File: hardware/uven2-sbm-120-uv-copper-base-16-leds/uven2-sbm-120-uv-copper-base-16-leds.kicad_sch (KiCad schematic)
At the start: 60 parts, among them J1 LED0+, J10 LED4-, J11 LED5+, J12 LED5-, J13 LED6+, J14 LED6-, J15 LED7+, J16 LED7-, J17 LED8+, J18 LED8-, J19 LED9+, J2 LED0-, J20 LED9-, J21 LED10+, J22 LED10-, J23 LED11+, J24 LED11-, J25 LED12+, J26 LED12-, J27 LED13+, J28 LED13-, J29 LED14+, J3 LED1+, J30 LED14-, J31 LED15+, J32 LED15-, J4 LED1-, J5 LED2+, J6 LED2-, J7 LED3+, J8 LED3-, J9 LED4+, U1 SBM-120-UV, U10 SBM-120-UV, U11 SBM-120-UV, U12 SBM-120-UV, U13 SBM-120-UV, U14 SBM-120-UV, U15 SBM-120-UV, U16 SBM-120-UV, U2 SBM-120-UV, U3 SBM-120-UV, U4 SBM-120-UV, U5 SBM-120-UV, U6 SBM-120-UV, U7 SBM-120-UV, U8 SBM-120-UV, U9 SBM-120-UV

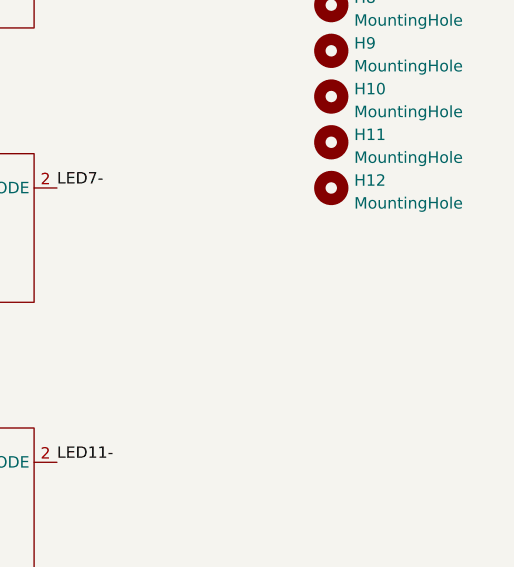
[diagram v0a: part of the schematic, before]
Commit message: more mounting holes
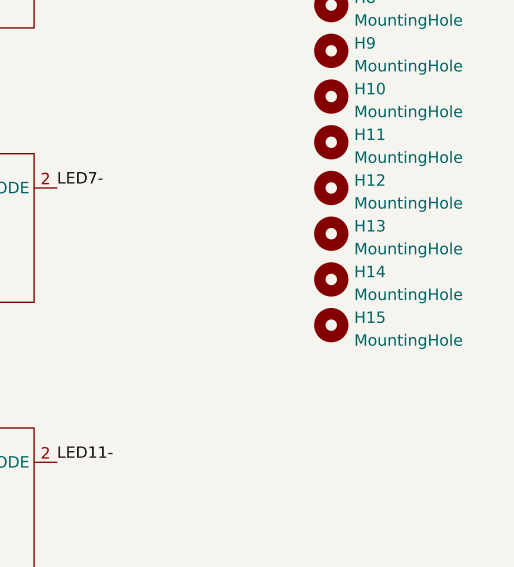
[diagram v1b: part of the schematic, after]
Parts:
- added H13, H14, H15: MountingHole, MountingHole:MountingHole_3.2mm_M3, symbol Mechanical:MountingHole
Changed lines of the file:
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@@
     (effects (font (size 1.27 1.27)) (justify left bottom))
+  )
+  (symbol (lib_id "Mechanical:MountingHole") (at 259.08 91.44 0) (unit 1)
+    (in_bom yes) (on_board yes) (fields_autoplaced)
+    (property "Reference" "H15" (id 0) (at 261.62 90.6053 0)
+      (effects (font (size 1.27 1.27)) (justify left))
+    )
+    (property "Value" "MountingHole" (id 1) (at 261.62 93.1422 0)
+      (effects (font (size 1.27 1.27)) (justify left))
+    )
+    (property "Footprint" "MountingHole:MountingHole_3.2mm_M3" (id 2) (at 259.08 91.44 0)
+      (effects (font (size 1.27 1.27)) hide)
+    )
+    (property "Datasheet" "~" (id 3) (at 259.08 91.44 0)
+      (effects (font (size 1.27 1.27)) hide)
+    )
   )
   (symbol (lib_id "custom:SBM-120-UV") (at 215.9 50.8 0) (unit 1)
@@
     (pin "1")
   )
+  (symbol (lib_id "Mechanical:MountingHole") (at 259.08 86.36 0) (unit 1)
+    (in_bom yes) (on_board yes) (fields_autoplaced)
+    (property "Reference" "H14" (id 0) (at 261.62 85.5253 0)
+      (effects (font (size 1.27 1.27)) (justify left))
+    )
+    (property "Value" "MountingHole" (id 1) (at 261.62 88.0622 0)
+      (effects (font (size 1.27 1.27)) (justify left))
+    )
+    (property "Footprint" "MountingHole:MountingHole_3.2mm_M3" (id 2) (at 259.08 86.36 0)
+      (effects (font (size 1.27 1.27)) hide)
+    )
+    (property "Datasheet" "~" (id 3) (at 259.08 86.36 0)
+      (effects (font (size 1.27 1.27)) hide)
+    )
+  )
   (symbol (lib_id "Connector:Conn_01x01_Female") (at 53.34 68.58 180) (unit 1)
     (in_bom yes) (on_board yes) (fields_autoplaced)
@@
     (pin "1")
   )
+  (symbol (lib_id "Mechanical:MountingHole") (at 259.08 81.28 0) (unit 1)
+    (in_bom yes) (on_board yes) (fields_autoplaced)
+    (property "Reference" "H13" (id 0) (at 261.62 80.4453 0)
+      (effects (font (size 1.27 1.27)) (justify left))
+    )
+    (property "Value" "MountingHole" (id 1) (at 261.62 82.9822 0)
+      (effects (font (size 1.27 1.27)) (justify left))
+    )
+    (property "Footprint" "MountingHole:MountingHole_3.2mm_M3" (id 2) (at 259.08 81.28 0)
+      (effects (font (size 1.27 1.27)) hide)
+    )
+    (property "Datasheet" "~" (id 3) (at 259.08 81.28 0)
+      (effects (font (size 1.27 1.27)) hide)
+    )
+  )
   (symbol (lib_id "Connector:Conn_01x01_Female") (at 53.34 43.18 180) (unit 1)
     (in_bom yes) (on_board yes) (fields_autoplaced)
@@
       (reference "H12") (unit 1) (value "MountingHole") (footprint "MountingHole:MountingHole_3.2mm_M3")
     )
+    (path "/480cf691-721f-4899-bd8b-114328ed6cb5"
+      (reference "H13") (unit 1) (value "MountingHole") (footprint "MountingHole:MountingHole_3.2mm_M3")
+    )
+    (path "/1b30173e-3e23-4824-b9c7-bba22dbc95f5"
+      (reference "H14") (unit 1) (value "MountingHole") (footprint "MountingHole:MountingHole_3.2mm_M3")
+    )
+    (path "/0d2686f8-8d34-493a-8a4f-3bd8bf6ef14b"
+      (reference "H15") (unit 1) (value "MountingHole") (footprint "MountingHole:MountingHole_3.2mm_M3")
+    )
     (path "/babefa49-307d-4cb6-8ca1-f2ed9a23079d"

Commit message: with thermistors
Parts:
- added H? (x5): MountingHole, MountingHole:MountingHole_3.2mm_M3, symbol Mechanical:MountingHole
- added J34: TEMP_LED0, TestPoint:TestPoint_Pad_2.0x2.0mm, symbol Connector:Conn_01x01_Female
- added J35: TEMP_LED1, TestPoint:TestPoint_Pad_2.0x2.0mm, symbol Connector:Conn_01x01_Female
- added J36: TEMP_LED2, TestPoint:TestPoint_Pad_2.0x2.0mm, symbol Connector:Conn_01x01_Female
- added J37: TEMP_LED3, TestPoint:TestPoint_Pad_2.0x2.0mm, symbol Connector:Conn_01x01_Female
- added J38: TEMP_LED4, TestPoint:TestPoint_Pad_2.0x2.0mm, symbol Connector:Conn_01x01_Female
- added J39: TEMP_LED5, TestPoint:TestPoint_Pad_2.0x2.0mm, symbol Connector:Conn_01x01_Female
- added J40: TEMP_LED6, TestPoint:TestPoint_Pad_2.0x2.0mm, symbol Connector:Conn_01x01_Female
- added J41: TEMP_LED7, TestPoint:TestPoint_Pad_2.0x2.0mm, symbol Connector:Conn_01x01_Female
- added J42: TEMP_LED8, TestPoint:TestPoint_Pad_2.0x2.0mm, symbol Connector:Conn_01x01_Female
- added J43: TEMP_LED9, TestPoint:TestPoint_Pad_2.0x2.0mm, symbol Connector:Conn_01x01_Female
- added J44: TEMP_LED10, TestPoint:TestPoint_Pad_2.0x2.0mm, symbol Connector:Conn_01x01_Female
- added J45: TEMP_LED11, TestPoint:TestPoint_Pad_2.0x2.0mm, symbol Connector:Conn_01x01_Female
- added J46: TEMP_LED12, TestPoint:TestPoint_Pad_2.0x2.0mm, symbol Connector:Conn_01x01_Female
- added J47: TEMP_LED13, TestPoint:TestPoint_Pad_2.0x2.0mm, symbol Connector:Conn_01x01_Female
- added J48: TEMP_LED14, TestPoint:TestPoint_Pad_2.0x2.0mm, symbol Connector:Conn_01x01_Female
- added J49: TEMP_LED15, TestPoint:TestPoint_Pad_2.0x2.0mm, symbol Connector:Conn_01x01_Female
- added J50, J51, J52, J53, J54, J55, J56, J57, J58, J59, J60, J61, J62, J63, J64, J65: GND, TestPoint:TestPoint_Pad_2.0x2.0mm, symbol Connector:Conn_01x01_Female
- added TH1, TH10, TH11, TH12, TH13, TH14, TH15, TH16, TH2, TH3, TH4, TH5, TH6, TH7, TH8, TH9: NTC, Resistor_SMD:R_0805_2012Metric_Pad1.20x1.40mm_HandSolder, symbol Device:Thermistor_NTC
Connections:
- new net: J39.1 (Pin_1), TH6.1
- new net: J36.1 (Pin_1), TH3.1
- new net: J41.1 (Pin_1), TH8.1
- new net: J43.1 (Pin_1), TH10.1
- new net: J48.1 (Pin_1), TH15.1
- new net: J47.1 (Pin_1), TH14.1
- new net: J49.1 (Pin_1), TH16.1
- new net: J44.1 (Pin_1), TH11.1
- new net: J37.1 (Pin_1), TH4.1
- new net: J40.1 (Pin_1), TH7.1
- new net: J35.1 (Pin_1), TH2.1
- new net: J38.1 (Pin_1), TH5.1
- new net: J46.1 (Pin_1), TH13.1
- new net: J34.1 (Pin_1), TH1.1
- new net: J42.1 (Pin_1), TH9.1
- new net: J45.1 (Pin_1), TH12.1
- new net GND: J50.1 (Pin_1), J51.1 (Pin_1), J52.1 (Pin_1), J53.1 (Pin_1), J54.1 (Pin_1), J55.1 (Pin_1), J56.1 (Pin_1), J57.1 (Pin_1), J58.1 (Pin_1), J59.1 (Pin_1), J60.1 (Pin_1), J61.1 (Pin_1), J62.1 (Pin_1), J63.1 (Pin_1), J64.1 (Pin_1), J65.1 (Pin_1), TH1.2, TH10.2, TH11.2, TH12.2, TH13.2, TH14.2, TH15.2, TH16.2, TH2.2, TH3.2, TH4.2, TH5.2, TH6.2, TH7.2, TH8.2, TH9.2
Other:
- moved on the sheet: J1, J10, J11, J12, J13, J14, J15, J16, J17, J18, J19, J2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

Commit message: with thermistors
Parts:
- gave numbers to parts that had none: 5
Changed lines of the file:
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@@
   (symbol (lib_id "Mechanical:MountingHole") (at 259.08 107.315 0) (unit 1)
     (in_bom yes) (on_board yes) (fields_autoplaced)
-    (property "Reference" "H?" (id 0) (at 261.62 106.4803 0)
+    (property "Reference" "H18" (id 0) (at 261.62 106.4803 0)
       (effects (font (size 1.27 1.27)) (justify left))
     )
@@
   (symbol (lib_id "Mechanical:MountingHole") (at 259.08 97.155 0) (unit 1)
     (in_bom yes) (on_board yes) (fields_autoplaced)
-    (property "Reference" "H?" (id 0) (at 261.62 96.3203 0)
+    (property "Reference" "H16" (id 0) (at 261.62 96.3203 0)
       (effects (font (size 1.27 1.27)) (justify left))
     )
@@
   (symbol (lib_id "Mechanical:MountingHole") (at 259.08 112.395 0) (unit 1)
     (in_bom yes) (on_board yes) (fields_autoplaced)
-    (property "Reference" "H?" (id 0) (at 261.62 111.5603 0)
+    (property "Reference" "H19" (id 0) (at 261.62 111.5603 0)
       (effects (font (size 1.27 1.27)) (justify left))
     )
@@
   (symbol (lib_id "Mechanical:MountingHole") (at 259.08 117.475 0) (unit 1)
     (in_bom yes) (on_board yes) (fields_autoplaced)
-    (property "Reference" "H?" (id 0) (at 261.62 116.6403 0)
+    (property "Reference" "H20" (id 0) (at 261.62 116.6403 0)
       (effects (font (size 1.27 1.27)) (justify left))
     )
@@
   (symbol (lib_id "Mechanical:MountingHole") (at 259.08 102.235 0) (unit 1)
     (in_bom yes) (on_board yes) (fields_autoplaced)
-    (property "Reference" "H?" (id 0) (at 261.62 101.4003 0)
+    (property "Reference" "H17" (id 0) (at 261.62 101.4003 0)
       (effects (font (size 1.27 1.27)) (justify left))
     )
@@
       (reference "H15") (unit 1) (value "MountingHole") (footprint "MountingHole:MountingHole_3.2mm_M3")
     )
+    (path "/741716d0-a841-4c1f-b24a-95f2ab48fc46"
+      (reference "H16") (unit 1) (value "MountingHole") (footprint "MountingHole:MountingHole_3.2mm_M3")
+    )
+    (path "/f5f59cc5-295d-452f-b22c-723c92bfdb2b"
+      (reference "H17") (unit 1) (value "MountingHole") (footprint "MountingHole:MountingHole_3.2mm_M3")
+    )
     (path "/1be9032b-da63-43b5-b4d8-9b92c8dcb60c"
-      (reference "H?") (unit 1) (value "MountingHole") (footprint "MountingHole:MountingHole_3.2mm_M3")
-    )
-    (path "/741716d0-a841-4c1f-b24a-95f2ab48fc46"
-      (reference "H?") (unit 1) (value "MountingHole") (footprint "MountingHole:MountingHole_3.2mm_M3")
+      (reference "H18") (unit 1) (value "MountingHole") (footprint "MountingHole:MountingHole_3.2mm_M3")
     )
     (path "/b7174d26-5625-4574-8691-f3e906654bf4"
-      (reference "H?") (unit 1) (value "MountingHole") (footprint "MountingHole:MountingHole_3.2mm_M3")
+      (reference "H19") (unit 1) (value "MountingHole") (footprint "MountingHole:MountingHole_3.2mm_M3")
     )
     (path "/cb7777f4-fc3c-4122-b581-d4c76e342d52"
-      (reference "H?") (unit 1) (value "MountingHole") (footprint "MountingHole:MountingHole_3.2mm_M3")
-    )
-    (path "/f5f59cc5-295d-452f-b22c-723c92bfdb2b"
-      (reference "H?") (unit 1) (value "MountingHole") (footprint "MountingHole:MountingHole_3.2mm_M3")
+      (reference "H20") (unit 1) (value "MountingHole") (footprint "MountingHole:MountingHole_3.2mm_M3")
     )
     (path "/babefa49-307d-4cb6-8ca1-f2ed9a23079d"

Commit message: ordered on jlcpcb
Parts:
- added FID1, FID2, FID3: Fiducial, Fiducial:Fiducial_1mm_Dia_2.54mm_Outer_CopperTop, symbol Mechanical:Fiducial
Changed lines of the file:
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@@
     (pin "2")
+  )
+  (symbol (lib_id "Mechanical:Fiducial") (at 207.01 142.875 0) (unit 1)
+    (in_bom yes) (on_board yes) (fields_autoplaced)
+    (property "Reference" "FID1" (id 0) (at 209.169 142.0403 0)
+      (effects (font (size 1.27 1.27)) (justify left))
+    )
+    (property "Value" "Fiducial" (id 1) (at 209.169 144.5772 0)
+      (effects (font (size 1.27 1.27)) (justify left))
+    )
+    (property "Footprint" "Fiducial:Fiducial_1mm_Dia_2.54mm_Outer_CopperTop" (id 2) (at 207.01 142.875 0)
+      (effects (font (size 1.27 1.27)) hide)
+    )
+    (property "Datasheet" "~" (id 3) (at 207.01 142.875 0)
+      (effects (font (size 1.27 1.27)) hide)
+    )
   )
   (symbol (lib_id "Connector:Conn_01x01_Female") (at 24.13 157.48 90) (unit 1)
@@
     (pin "2")
   )
+  (symbol (lib_id "Mechanical:Fiducial") (at 207.01 156.21 0) (unit 1)
+    (in_bom yes) (on_board yes) (fields_autoplaced)
+    (property "Reference" "FID3" (id 0) (at 209.169 155.3753 0)
+      (effects (font (size 1.27 1.27)) (justify left))
+    )
+    (property "Value" "Fiducial" (id 1) (at 209.169 157.9122 0)
+      (effects (font (size 1.27 1.27)) (justify left))
+    )
+    (property "Footprint" "Fiducial:Fiducial_1mm_Dia_2.54mm_Outer_CopperTop" (id 2) (at 207.01 156.21 0)
+      (effects (font (size 1.27 1.27)) hide)
+    )
+    (property "Datasheet" "~" (id 3) (at 207.01 156.21 0)
+      (effects (font (size 1.27 1.27)) hide)
+    )
+  )
   (symbol (lib_id "Mechanical:MountingHole") (at 259.08 71.12 0) (unit 1)
     (in_bom yes) (on_board yes) (fields_autoplaced)
@@
     (pin "1")
   )
+  (symbol (lib_id "Mechanical:Fiducial") (at 207.01 149.225 0) (unit 1)
+    (in_bom yes) (on_board yes) (fields_autoplaced)
+    (property "Reference" "FID2" (id 0) (at 209.169 148.3903 0)
+      (effects (font (size 1.27 1.27)) (justify left))
+    )
+    (property "Value" "Fiducial" (id 1) (at 209.169 150.9272 0)
+      (effects (font (size 1.27 1.27)) (justify left))
+    )
+    (property "Footprint" "Fiducial:Fiducial_1mm_Dia_2.54mm_Outer_CopperTop" (id 2) (at 207.01 149.225 0)
+      (effects (font (size 1.27 1.27)) hide)
+    )
+    (property "Datasheet" "~" (id 3) (at 207.01 149.225 0)
+      (effects (font (size 1.27 1.27)) hide)
+    )
+  )
   (symbol (lib_id "power:GND") (at 106.68 190.5 0) (unit 1)
     (in_bom yes) (on_board yes) (fields_autoplaced)
@@
       (reference "#PWR0133") (unit 1) (value "GND") (footprint "")
     )
+    (path "/686adb78-b53f-4d78-b9b6-4e8063336041"
+      (reference "FID1") (unit 1) (value "Fiducial") (footprint "Fiducial:Fiducial_1mm_Dia_2.54mm_Outer_CopperTop")
+    )
+    (path "/eb13c41a-991f-400e-b1a6-ad52e3bec075"
+      (reference "FID2") (unit 1) (value "Fiducial") (footprint "Fiducial:Fiducial_1mm_Dia_2.54mm_Outer_CopperTop")
+    )
+    (path "/c4cc3f36-a208-4860-a560-60916ebae22c"
+      (reference "FID3") (unit 1) (value "Fiducial") (footprint "Fiducial:Fiducial_1mm_Dia_2.54mm_Outer_CopperTop")
+    )
     (path "/f86cffa0-62d2-47d5-a433-d87c37296089"
